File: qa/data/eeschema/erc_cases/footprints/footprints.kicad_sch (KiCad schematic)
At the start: 3 parts, among them U1 DUAL

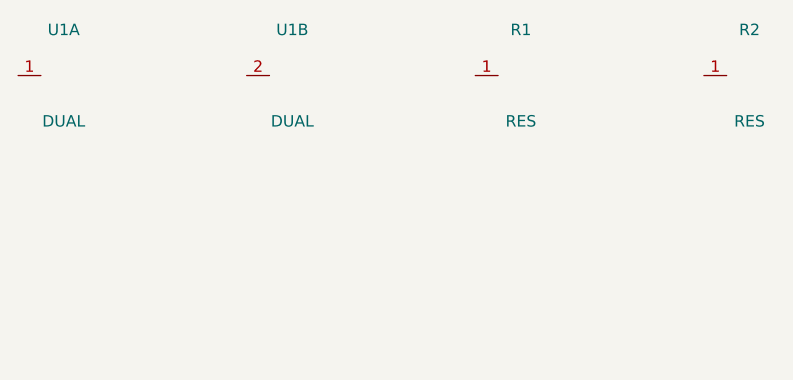
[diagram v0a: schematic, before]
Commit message: qa: extend four ERC fixtures to reach what the S2-4b-7/8 sweep found unpinned
similar_labels gains a subsheet with a local daTa (case variants on two sheets are fine),
similar_power an ordinary part valued gnd (only power pins compare), symbol_pins a twin
whose duplicate pin numbers are jumpers, footprints a unit with no footprint and a
Resistor_SMD:R_* filter (a ':' filter matches the whole id). kicad-cli regenerated
every report; all match.

Co-Authored-By: Claude Opus 5.5 (1M context) <noreply@anthropic.com>
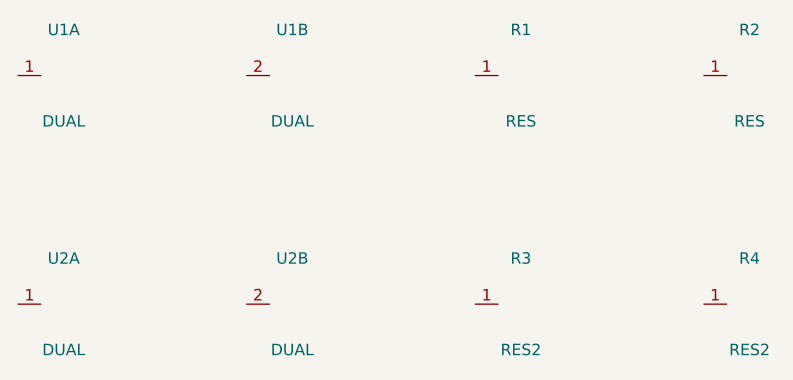
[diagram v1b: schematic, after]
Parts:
- added R3: RES2, Resistor_SMD:R_0402, symbol erc:RES2
- added R4: RES2, Other:R_0402, symbol erc:RES2
- added U2: DUAL, Package_SO:SOIC-8, symbol erc:DUAL
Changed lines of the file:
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@@
 		(instances (project "footprints" (path "/61111111-2222-3333-4444-555555555555" (reference "R2") (unit 1))))
+	)
+	(symbol (lib_id "erc:DUAL") (at 50.8 127 0) (unit 1) (body_style 1) (exclude_from_sim no) (in_bom yes) (on_board yes) (dnp no)
+		(property "Reference" "U2" (at 50.8 121.92 0) (effects (font (size 1.27 1.27))))
+		(property "Value" "DUAL" (at 50.8 132.08 0) (effects (font (size 1.27 1.27))))
+		(property "Footprint" "Package_SO:SOIC-8" (at 50.8 127 0) (hide yes) (effects (font (size 1.27 1.27))))
+		(property "Datasheet" "" (at 50.8 127 0) (hide yes) (effects (font (size 1.27 1.27))))
+		(pin "1")
+		(pin "2")
+		(instances (project "footprints" (path "/61111111-2222-3333-4444-555555555555" (reference "U2") (unit 1))))
+	)
+	(symbol (lib_id "erc:DUAL") (at 76.2 127 0) (unit 2) (body_style 1) (exclude_from_sim no) (in_bom yes) (on_board yes) (dnp no)
+		(property "Reference" "U2" (at 76.2 121.92 0) (effects (font (size 1.27 1.27))))
+		(property "Value" "DUAL" (at 76.2 132.08 0) (effects (font (size 1.27 1.27))))
+		(property "Footprint" "" (at 76.2 127 0) (hide yes) (effects (font (size 1.27 1.27))))
+		(property "Datasheet" "" (at 76.2 127 0) (hide yes) (effects (font (size 1.27 1.27))))
+		(pin "1")
+		(pin "2")
+		(instances (project "footprints" (path "/61111111-2222-3333-4444-555555555555" (reference "U2") (unit 2))))
+	)
+	(symbol (lib_id "erc:RES2") (at 101.6 127 0) (unit 1) (body_style 1) (exclude_from_sim no) (in_bom yes) (on_board yes) (dnp no)
+		(property "Reference" "R3" (at 101.6 121.92 0) (effects (font (size 1.27 1.27))))
+		(property "Value" "RES2" (at 101.6 132.08 0) (effects (font (size 1.27 1.27))))
+		(property "Footprint" "Resistor_SMD:R_0402" (at 101.6 127 0) (hide yes) (effects (font (size 1.27 1.27))))
+		(property "Datasheet" "" (at 101.6 127 0) (hide yes) (effects (font (size 1.27 1.27))))
+		(pin "1")
+		(instances (project "footprints" (path "/61111111-2222-3333-4444-555555555555" (reference "R3") (unit 1))))
+	)
+	(symbol (lib_id "erc:RES2") (at 127 127 0) (unit 1) (body_style 1) (exclude_from_sim no) (in_bom yes) (on_board yes) (dnp no)
+		(property "Reference" "R4" (at 127 121.92 0) (effects (font (size 1.27 1.27))))
+		(property "Value" "RES2" (at 127 132.08 0) (effects (font (size 1.27 1.27))))
+		(property "Footprint" "Other:R_0402" (at 127 127 0) (hide yes) (effects (font (size 1.27 1.27))))
+		(property "Datasheet" "" (at 127 127 0) (hide yes) (effects (font (size 1.27 1.27))))
+		(pin "1")
+		(instances (project "footprints" (path "/61111111-2222-3333-4444-555555555555" (reference "R4") (unit 1))))
 	)
 	(sheet_instances (path "/" (page "1")))
